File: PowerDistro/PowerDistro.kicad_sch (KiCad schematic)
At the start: 8 parts

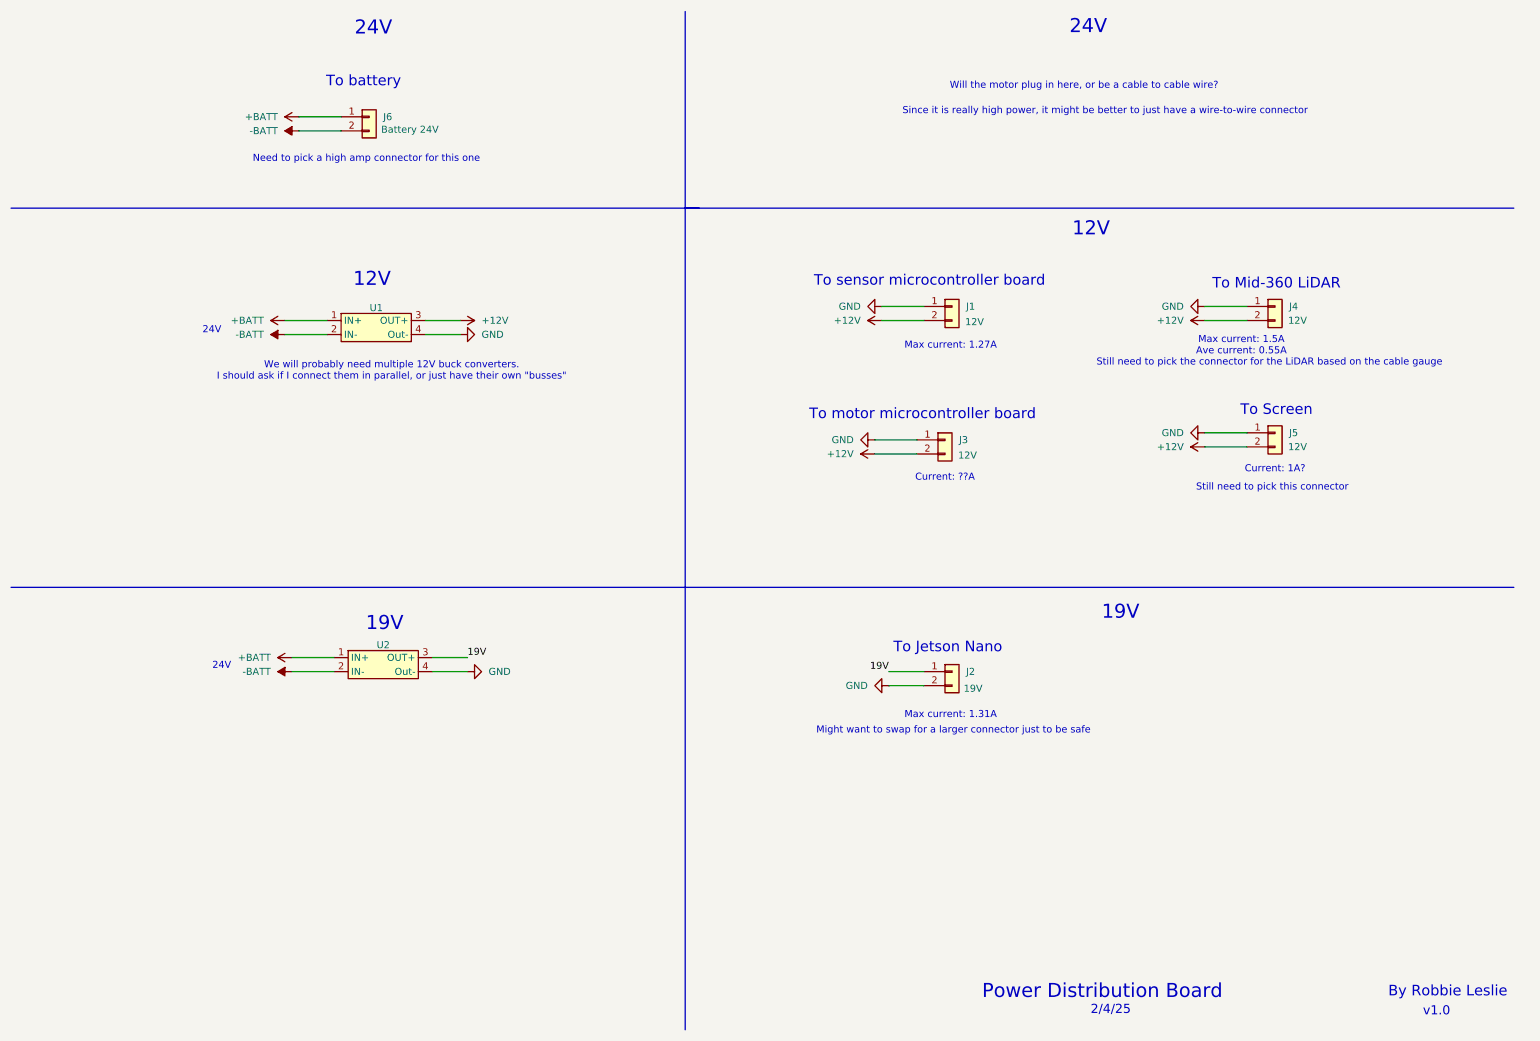
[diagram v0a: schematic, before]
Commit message: Added a second 12V converter
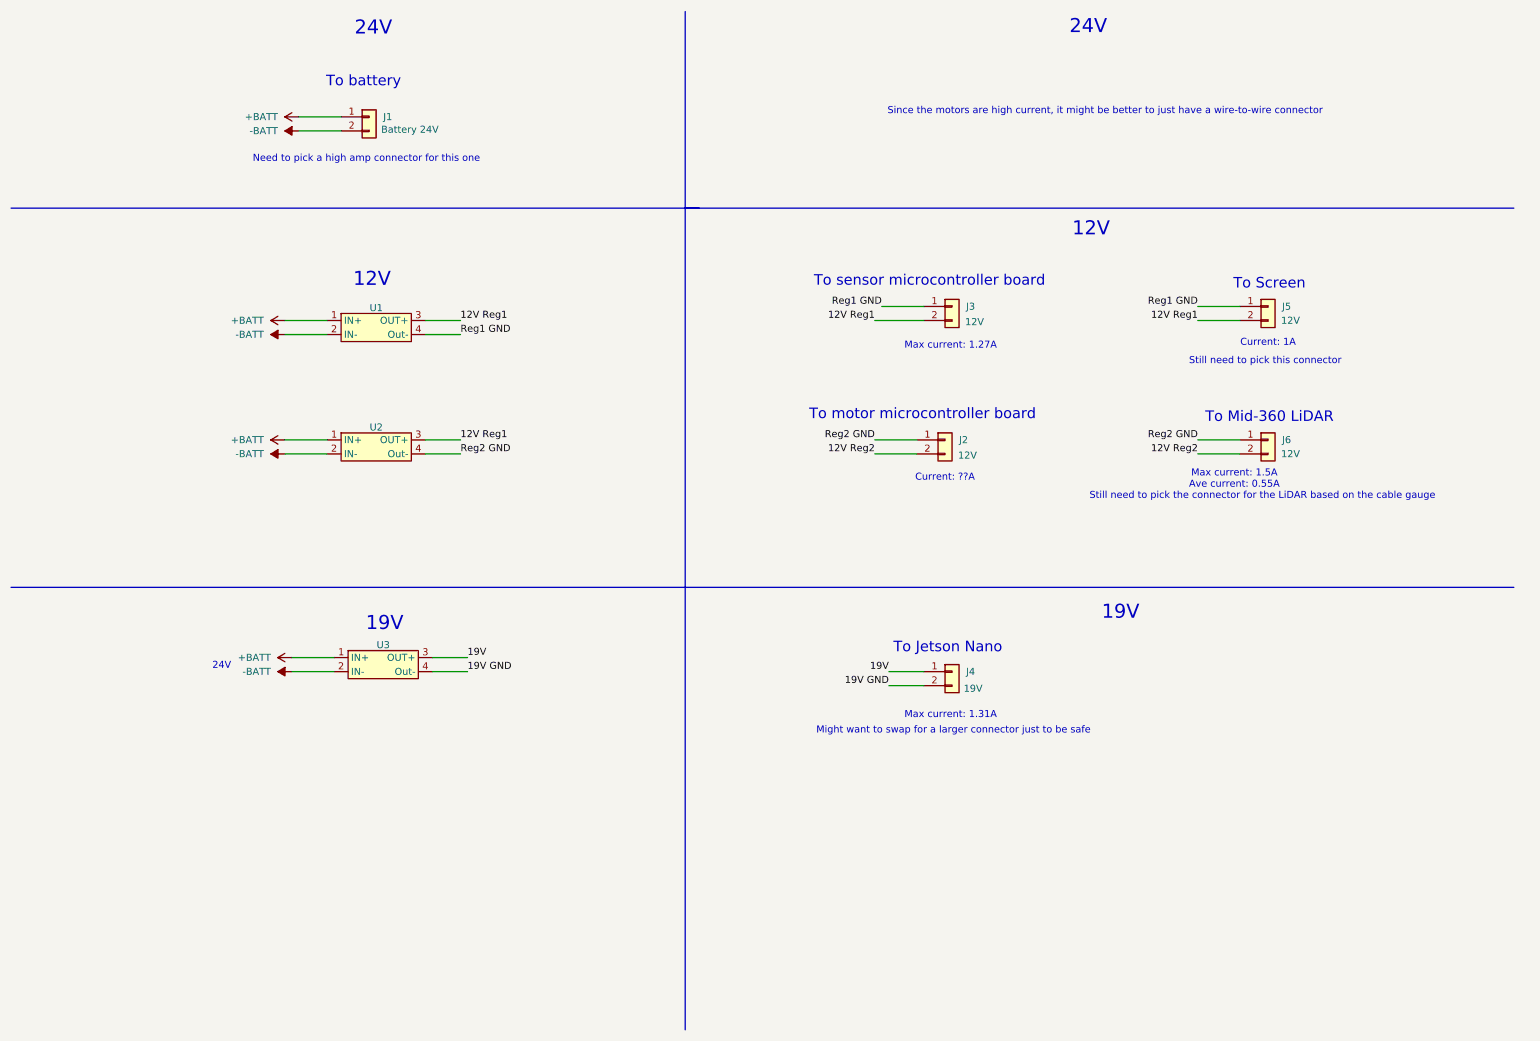
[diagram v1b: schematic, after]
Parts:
- added U2: ~, symbol Regulator_Boards:LM2596
- renumbered J6 to J1, J3 to J2, J1 to J3, J2 to J4, J4 to J6, U2 to U3
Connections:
- net +BATT: now also U2.1 (IN+)
- net -BATT: now also U2.2 (IN-)
- net +12V renamed 12V Reg1
- net 12V Reg1: now also U2.3 (OUT+); no longer J2.2 (Pin_2), J6.2 (Pin_2)
- removed net GND: J2.1 (Pin_1), J3.1 (Pin_1), J4.2 (Pin_2), J5.1 (Pin_1), J6.1 (Pin_1), U1.4 (Out-), U3.4 (Out-)
- new net 12V Reg2: J2.2 (Pin_2), J6.2 (Pin_2)
- new net 19V GND: J4.2 (Pin_2), U3.4 (Out-)
- new net Reg1 GND: J3.1 (Pin_1), J5.1 (Pin_1), U1.4 (Out-)
- new net Reg2 GND: J2.1 (Pin_1), J6.1 (Pin_1), U2.4 (Out-)
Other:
- note added: "Current: 1A"
- note added: "Since the motors are high current, it might be better to just have a wire-to-wire connector"
- note removed: "2/4/25"
- note removed: "By Robbie Leslie"
- note removed: "Current: 1A?"
- note removed: "Power Distribution Board"
- note removed: "Since it is really high power, it might be better to just have a wire-to-wire connector"
- note removed: "We will probably need multiple 12V buck converters. I should ask if I connect them in parallel, or just have their own "busses""
- note removed: "Will the motor plug in here, or be a cable to cable wire?"
- note removed: "v1.0"
- company: (none) -> Lafyaette College
- title: (none) -> Power Distribution Board
- moved on the sheet: J5, J6

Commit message: Finished picking connectors and started working on layout
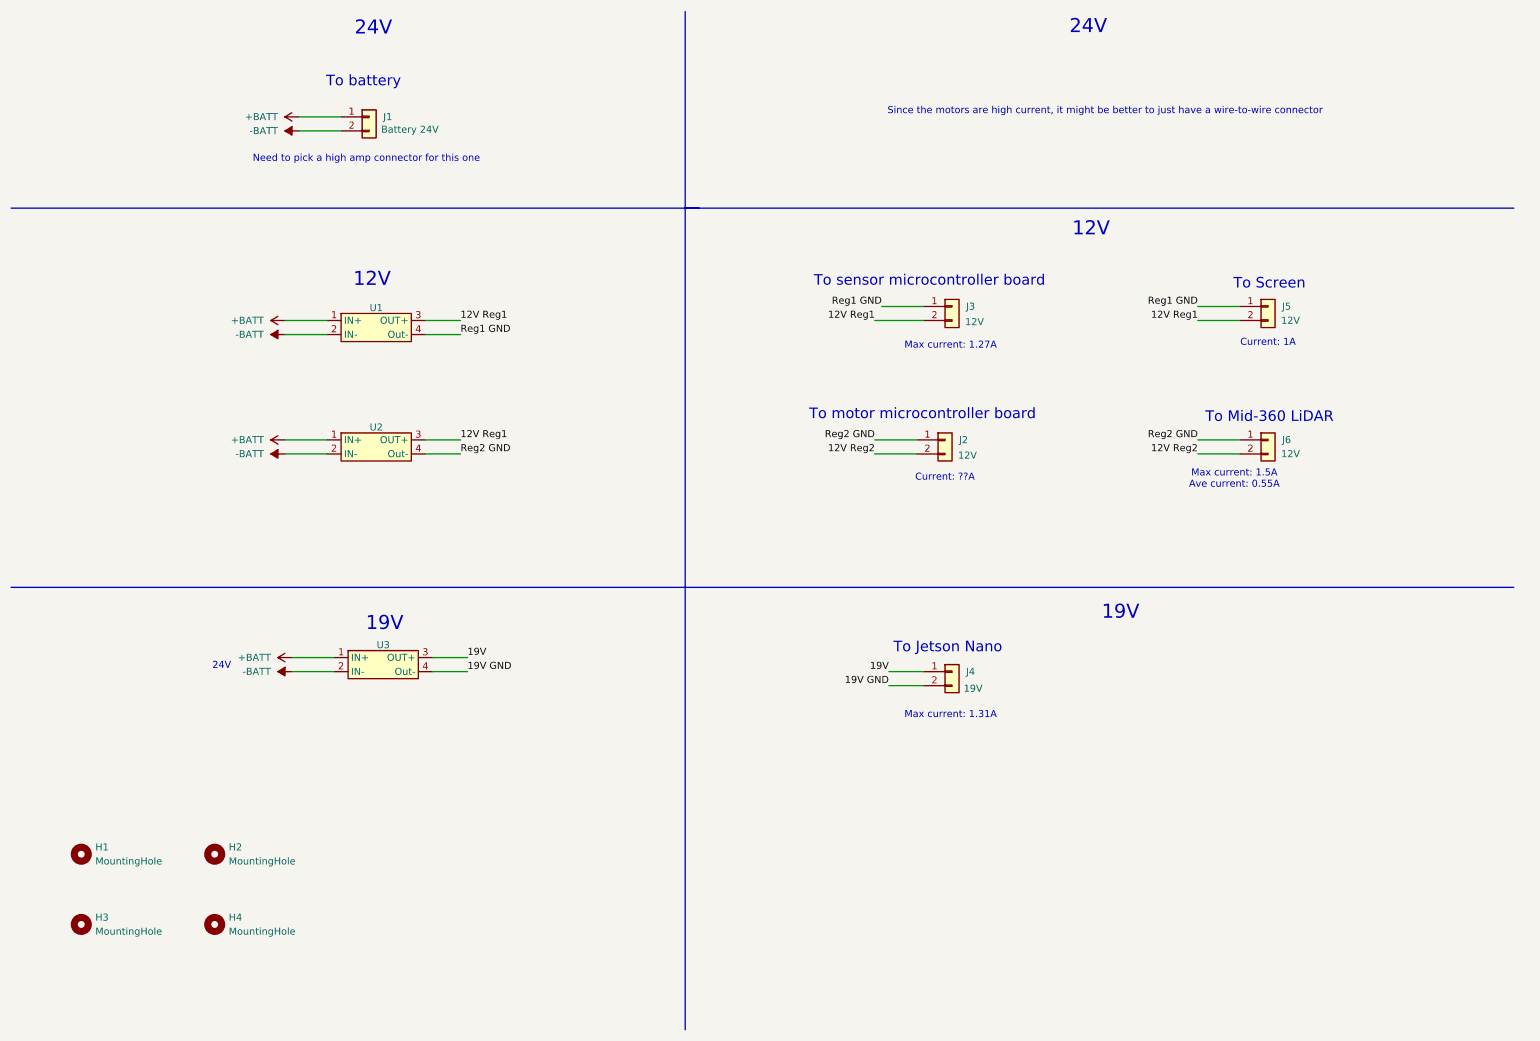
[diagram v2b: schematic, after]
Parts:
- added H1, H2, H3, H4: MountingHole, MountingHole:MountingHole_3.2mm_M3_ISO7380_Pad, symbol Mechanical:MountingHole
- J1: footprint (none) -> Connector_Molex:Molex_Mini-Fit_Jr_5566-02A_2x01_P4.20mm_Vertical; Manufacturer Part Number (none) -> 0039290023
- J4: Manufacturer Part Number (none) -> S2B-XH-A-1
- J5, J6: footprint (none) -> Connector_JST:JST_XH_S2B-XH-A_1x02_P2.50mm_Horizontal; Manufacturer Part Number (none) -> S2B-XH-A-1
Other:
- note removed: "Might want to swap for a larger connector just to be safe"
- note removed: "Still need to pick the connector for the LiDAR based on the cable gauge"
- note removed: "Still need to pick this connector"

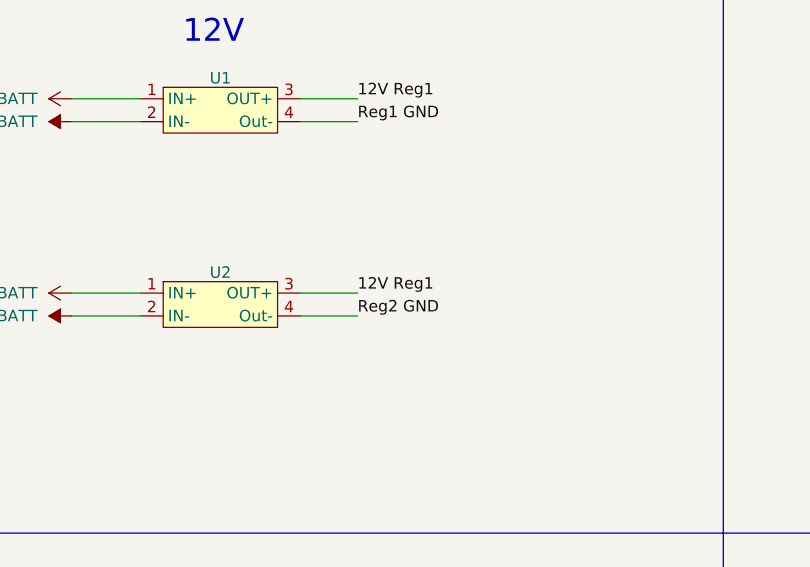
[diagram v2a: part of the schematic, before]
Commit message: Finished initial layout
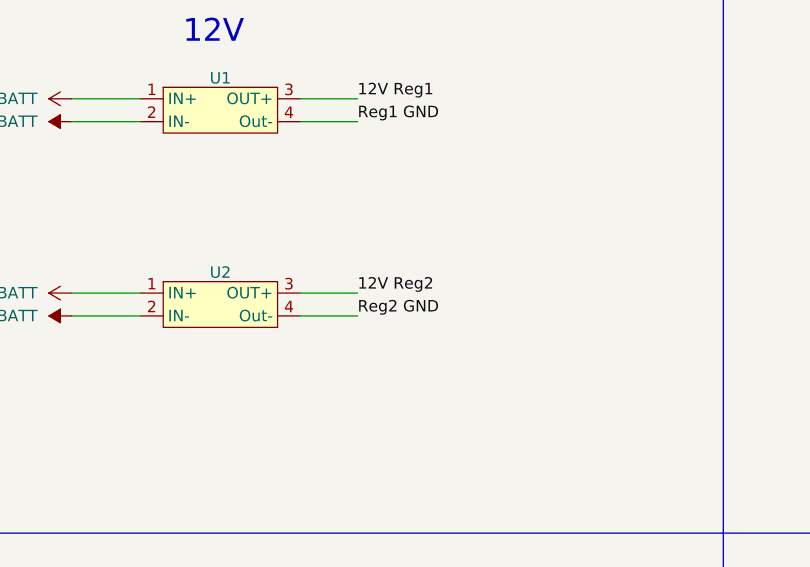
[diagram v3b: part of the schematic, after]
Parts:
- J1: Connects To (none) -> 24V Battery
- J2: Connects To (none) -> Motor Microcontroller
- J3: Connects To (none) -> Sensor Microcontroller
- J4: Connects To (none) -> Jetson Nano
- J5: Connects To (none) -> Screen
- J6: Connects To (none) -> LiDAR
- U1, U2, U3: footprint (none) -> Regulator_Boards:LM2596
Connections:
- net 12V Reg1: no longer U2.3 (OUT+)
- net 12V Reg2: now also U2.3 (OUT+)
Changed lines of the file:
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@@
 		)
 	)
-	(label "12V Reg1"
+	(label "12V Reg2"
 		(at 93.98 90.17 0)
 		(effects
@@
 			)
 		)
+		(property "Connects To" ""
+			(at 25.4 165.1 0)
+			(effects
+				(font
+					(size 1.27 1.27)
+				)
+				(hide yes)
+			)
+		)
 		(instances
 			(project ""
@@
 		)
 		(property "Manufacturer Part Number" "0039290023"
+			(at 77.47 31.75 0)
+			(effects
+				(font
+					(size 1.27 1.27)
+				)
+				(hide yes)
+			)
+		)
+		(property "Connects To" "24V Battery"
 			(at 77.47 31.75 0)
 			(effects
@@
 			)
 		)
+		(property "Connects To" ""
+			(at 49.53 165.1 0)
+			(effects
+				(font
+					(size 1.27 1.27)
+				)
+				(hide yes)
+			)
+		)
 		(instances
 			(project "PowerDistro"
@@
 			)
 		)
+		(property "Connects To" ""
+			(at 25.4 177.8 0)
+			(effects
+				(font
+					(size 1.27 1.27)
+				)
+				(hide yes)
+			)
+		)
 		(instances
 			(project "PowerDistro"
@@
 		)
 		(property "Description" "Mounting Hole without connection"
+			(at 49.53 177.8 0)
+			(effects
+				(font
+					(size 1.27 1.27)
+				)
+				(hide yes)
+			)
+		)
+		(property "Connects To" ""
 			(at 49.53 177.8 0)
 			(effects
@@
 			)
 		)
-		(property "Footprint" ""
+		(property "Footprint" "Regulator_Boards:LM2596"
 			(at 78.74 69.85 0)
 			(effects
@@
 		)
 		(property "Description" ""
+			(at 78.74 69.85 0)
+			(effects
+				(font
+					(size 1.27 1.27)
+				)
+				(hide yes)
+			)
+		)
+		(property "Connects To" ""
 			(at 78.74 69.85 0)
 			(effects
@@
 			)
 		)
-		(property "Footprint" ""
+		(property "Footprint" "Regulator_Boards:LM2596"
 			(at 80.01 130.81 0)
 			(effects
@@
 		)
 		(property "Description" ""
+			(at 80.01 130.81 0)
+			(effects
+				(font
+					(size 1.27 1.27)
+				)
+				(hide yes)
+			)
+		)
+		(property "Connects To" ""
 			(at 80.01 130.81 0)
 			(effects
@@
 			)
 		)
+		(property "Connects To" "Jetson Nano"
+			(at 182.88 132.08 0)
+			(effects
+				(font
+					(size 1.27 1.27)
+				)
+				(hide yes)
+			)
+		)
 		(pin "2"
 		)
@@
 					(size 1.27 1.27)
 				)
+			)
+		)
+		(property "Connects To" "Motor Microcontroller"
+			(at 181.61 90.17 0)
+			(effects
+				(font
+					(size 1.27 1.27)
+				)
+				(hide yes)
 			)
 		)
@@
 			)
 		)
+		(property "Connects To" "LiDAR"
+			(at 240.03 90.17 0)
+			(effects
+				(font
+					(size 1.27 1.27)
+				)
+				(hide yes)
+			)
+		)
 		(pin "2"
 		)
@@
 					(size 1.27 1.27)
 				)
+			)
+		)
+		(property "Connects To" "Sensor Microcontroller"
+			(at 182.88 66.04 0)
+			(effects
+				(font
+					(size 1.27 1.27)
+				)
+				(hide yes)
 			)
 		)
@@
 			)
 		)
-		(property "Footprint" ""
+		(property "Footprint" "Regulator_Boards:LM2596"
 			(at 78.74 91.44 0)
 			(effects
@@
 			)
 		)
+		(property "Connects To" ""
+			(at 78.74 91.44 0)
+			(effects
+				(font
+					(size 1.27 1.27)
+				)
+				(hide yes)
+			)
+		)
 		(pin "3"
 		)
@@
 			(at 240.03 66.04 0)
 			(effects
+				(font
+					(size 1.27 1.27)
+				)
+				(hide yes)
+			)
+		)
+		(property "Connects To" "Screen"
+			(at 240.03 66.04 0)
+			(effects
